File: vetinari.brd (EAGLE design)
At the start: 99.1 x 38.1 mm, 26 parts, among them J1 ICSP, U1 ATtiny84A-SSU, U2 MCP79412, Y1 32.768 kHz

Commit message: v1 as sent to fab
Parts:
- C1: device _jc:M0805 -> _jc:M1206
- moved C1 2.67 mm to (29.1, 32.3), turned to 90 degrees
- moved R2 0.72 mm to (25.7, 30.1)
- moved R3 0.57 mm to (22.9, 30.1)
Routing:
- net VCC: track 79.1 -> 75.5 mm
- net SCK/SCL: track 36.7 -> 37.6 mm
- net MOSI/SDA: track 34.9 -> 34.4 mm
- net GND: vias 12 -> 15

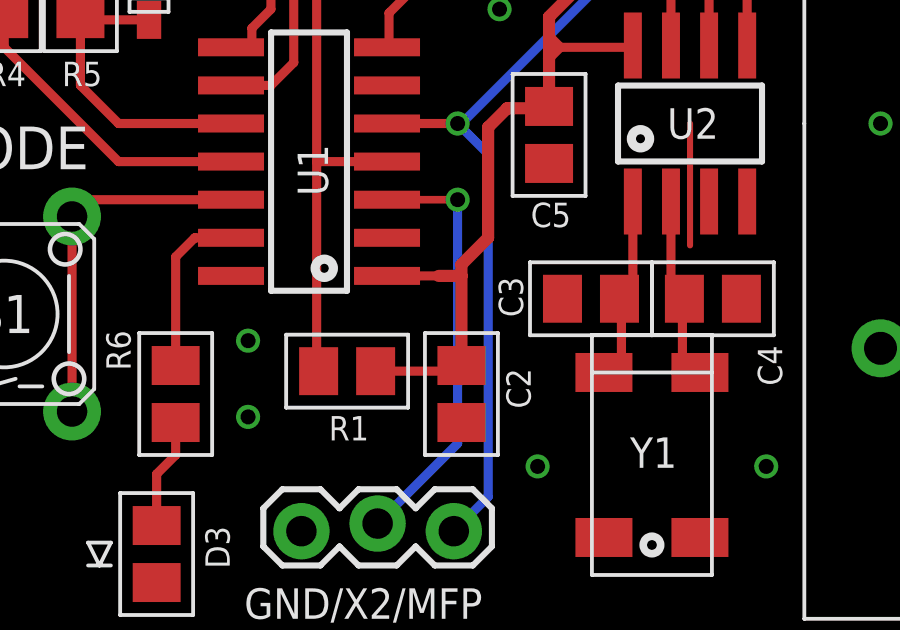
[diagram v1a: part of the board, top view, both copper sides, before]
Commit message: Tweak trace on board, add .txt doc files and .png images.
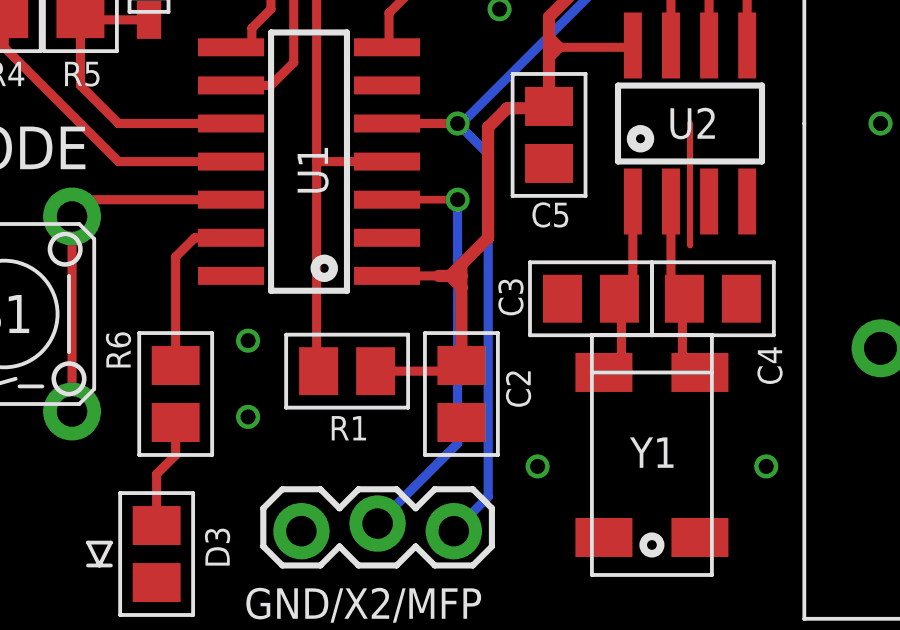
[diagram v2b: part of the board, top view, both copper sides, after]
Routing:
- net VCC: track 75.5 -> 76.6 mm
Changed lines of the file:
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@@
 <wire x1="17.46" y1="9.525" x2="20.132" y2="9.525" width="0.3048" layer="1"/>
 <wire x1="20.132" y1="9.525" x2="20.32" y2="9.713" width="0.3048" layer="1"/>
-<wire x1="20.32" y1="9.713" x2="20.32" y2="12.7" width="0.4064" layer="1"/>
+<wire x1="20.32" y1="9.713" x2="20.32" y2="12.319" width="0.4064" layer="1"/>
+<wire x1="20.32" y1="12.319" x2="20.32" y2="12.7" width="0.4064" layer="1"/>
 <wire x1="20.32" y1="12.7" x2="20.32" y2="13.081" width="0.4064" layer="1"/>
 <wire x1="20.32" y1="13.081" x2="21.209" y2="13.97" width="0.4064" layer="1"/>
-<wire x1="19.558" y1="12.7" x2="20.32" y2="12.7" width="0.4064" layer="1"/>
+<wire x1="19.558" y1="12.7" x2="19.939" y2="12.7" width="0.4064" layer="1"/>
 <contactref element="B2" pad="P1"/>
 <contactref element="B2" pad="P2"/>
+<wire x1="19.939" y1="12.7" x2="20.32" y2="12.7" width="0.4064" layer="1"/>
 <wire x1="45.466" y1="27.94" x2="37.846" y2="27.94" width="0.4064" layer="1"/>
 <wire x1="29.083" y1="30.858" x2="29.083" y2="28.321" width="0.4064" layer="1"/>
@@
 <wire x1="25.654" y1="31.049" x2="28.892" y2="31.049" width="0.4064" layer="1"/>
 <wire x1="28.892" y1="31.049" x2="29.083" y2="30.858" width="0.4064" layer="1"/>
+<wire x1="20.32" y1="13.081" x2="19.939" y2="12.7" width="0.4064" layer="1"/>
+<wire x1="19.939" y1="12.7" x2="20.32" y2="12.319" width="0.4064" layer="1"/>
 </signal>
 <signal name="GND">
@@
 </signal>
 </signals>
-<errors>
-</errors>
 </board>
 </drawing>
